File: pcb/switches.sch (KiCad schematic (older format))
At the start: 168 parts

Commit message: correct key sizes
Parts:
- MX_0_1, MX_1_1, MX_2_1, MX_3_1, MX_4_1, MX_5_1, MX_6_1, MX_7_1, MX_8_1, MX_9_1, MX_A_1, MX_B_1, MX_COMMA_1, MX_C_1, MX_DELETE_1, MX_DOT_1, MX_DOWN_1, MX_D_1, MX_END_1, MX_EQUALS_1, MX_ESC_1, MX_E_1, MX_F10_1, MX_F11_1, MX_F12_1, MX_F1_1, MX_F2_1, MX_F3_1, MX_F4_1, MX_F5_1, MX_F6_1, MX_F7_1, MX_F8_1, MX_F9_1, MX_FN_1, MX_F_1, MX_G_1, MX_HOME_1, MX_H_1, MX_I_1, MX_J_1, MX_K_1, MX_LBRAC_1, MX_LEFT_1, MX_L_1, MX_MINUS_1, MX_M_1, MX_N_1, MX_O_1, MX_PAUSE_1, MX_PGDN_1, MX_PGUP_1, MX_PRTSC_1, MX_P_1, MX_QUOTE_1, MX_Q_1, MX_RALT_1, MX_RBRAC_1, MX_RCTRL_1, MX_RIGHT_1, MX_R_1, MX_SEMIC_1, MX_SLASH_1, MX_S_1, MX_TILDE_1, MX_T_1, MX_UP_1, MX_U_1, MX_V_1, MX_W_1, MX_X_1, MX_Y_1, MX_Z_1: footprint (none) -> keys:MX-1U
- MX_BKSPACE_1: footprint (none) -> keys:MX-2U
- MX_BSLSH_1, MX_TAB_1: footprint (none) -> keys:MX-1.5U
- MX_CAPS_1, MX_RSHIFT_1: footprint (none) -> keys:MX-1.75U
- MX_ENTER_1, MX_LSHIFT_1: footprint (none) -> keys:MX-2.25U
- MX_LALT_1, MX_LCTRL_1, MX_OS_1: footprint (none) -> keys:MX-1.25U
- MX_SPACE_1: footprint (none) -> keys:MX-6.25U

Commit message: labels
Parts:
- added R? (x2), R_0_1, R_1_1, R_2_1, R_3_1, R_4_1, R_5_1, R_6_1, R_7_1, R_8_1, R_9_1, R_A_1, R_BKSPACE_1, R_BSLSH_1, R_B_1, R_CAPS_1, R_COMMA_1, R_C_1, R_DELETE_1, R_DOT_1, R_DOWN_1, R_D_1, R_END_1, R_ENTER_1, R_EQUALS_1, R_ESC_1, R_E_1, R_F10_1, R_F11_1, R_F12_1, R_F1_1, R_F2_1, R_F3_1, R_F4_1, R_F5_1, R_F7_1, R_F8_1, R_F9_1, R_FN_1, R_F_1, R_G_1, R_HOME_1, R_H_1, R_I_1, R_J_1, R_K_1, R_LALT_1, R_LBRAC_1, R_LCTRL_1, R_LEFT_1, R_LSHIFT_1, R_L_1, R_MINUS_1, R_M_1, R_N_1, R_OS_1, R_O_1, R_PAUSE_1, R_PGDN_1, R_PGUP_1, R_PRTSC_1, R_P_1, R_QUOTE_1, R_Q_1, R_RALT_1, R_RBRAC_1, R_RCTRL_1, R_RIGHT_1, R_RSHIFT_1, R_R_1, R_SEMIC_1, R_SLASH_1, R_SPACE_1, R_S_1, R_TAB_1, R_TILDE_1, R_T_1, R_UP_1, R_U_1, R_V_1, R_W_1, R_X_1, R_Y_1: R, symbol Device:R
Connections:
- net at MX_ESC_1.3 (LED): now also R_ESC_1.1
- net LEDGND: now reaches MX_ESC_1.4 (LEDGND)
- net LEDGND: now also MX_0_1.4 (LEDGND), MX_1_1.4 (LEDGND), MX_2_1.4 (LEDGND), MX_3_1.4 (LEDGND), MX_4_1.4 (LEDGND), MX_5_1.4 (LEDGND), MX_6_1.4 (LEDGND), MX_7_1.4 (LEDGND), MX_8_1.4 (LEDGND), MX_9_1.4 (LEDGND), MX_A_1.4 (LEDGND), MX_BKSPACE_1.4 (LEDGND), MX_BSLSH_1.4 (LEDGND), MX_B_1.4 (LEDGND), MX_CAPS_1.4 (LEDGND), MX_COMMA_1.4 (LEDGND), MX_C_1.4 (LEDGND), MX_DELETE_1.4 (LEDGND), MX_DOT_1.4 (LEDGND), MX_DOWN_1.4 (LEDGND), MX_D_1.4 (LEDGND), MX_END_1.4 (LEDGND), MX_ENTER_1.4 (LEDGND), MX_EQUALS_1.4 (LEDGND), MX_E_1.4 (LEDGND), MX_F10_1.4 (LEDGND), MX_F11_1.4 (LEDGND), MX_F12_1.4 (LEDGND), MX_F1_1.4 (LEDGND), MX_F2_1.4 (LEDGND), MX_F3_1.4 (LEDGND), MX_F4_1.4 (LEDGND), MX_F5_1.4 (LEDGND), MX_F6_1.4 (LEDGND), MX_F7_1.4 (LEDGND), MX_F8_1.4 (LEDGND), MX_F9_1.4 (LEDGND), MX_FN_1.4 (LEDGND), MX_F_1.4 (LEDGND), MX_G_1.4 (LEDGND), MX_HOME_1.4 (LEDGND), MX_H_1.4 (LEDGND), MX_I_1.4 (LEDGND), MX_J_1.4 (LEDGND), MX_K_1.4 (LEDGND), MX_LALT_1.4 (LEDGND), MX_LBRAC_1.4 (LEDGND), MX_LCTRL_1.4 (LEDGND), MX_LEFT_1.4 (LEDGND), MX_LSHIFT_1.4 (LEDGND), MX_L_1.4 (LEDGND), MX_MINUS_1.4 (LEDGND), MX_M_1.4 (LEDGND), MX_N_1.4 (LEDGND), MX_OS_1.4 (LEDGND), MX_O_1.4 (LEDGND), MX_PAUSE_1.4 (LEDGND), MX_PGDN_1.4 (LEDGND), MX_PGUP_1.4 (LEDGND), MX_PRTSC_1.4 (LEDGND), MX_P_1.4 (LEDGND), MX_QUOTE_1.4 (LEDGND), MX_Q_1.4 (LEDGND), MX_RALT_1.4 (LEDGND), MX_RBRAC_1.4 (LEDGND), MX_RCTRL_1.4 (LEDGND), MX_RIGHT_1.4 (LEDGND), MX_RSHIFT_1.4 (LEDGND), MX_R_1.4 (LEDGND), MX_SEMIC_1.4 (LEDGND), MX_SLASH_1.4 (LEDGND), MX_SPACE_1.4 (LEDGND), MX_S_1.4 (LEDGND), MX_TAB_1.4 (LEDGND), MX_TILDE_1.4 (LEDGND), MX_T_1.4 (LEDGND), MX_UP_1.4 (LEDGND), MX_U_1.4 (LEDGND), MX_V_1.4 (LEDGND), MX_W_1.4 (LEDGND), MX_X_1.4 (LEDGND), MX_Y_1.4 (LEDGND), MX_Z_1.4 (LEDGND)
- net at MX_F1_1.3 (LED): now also R_F1_1.1
- net at MX_F2_1.3 (LED): now also R_F2_1.1
- net at MX_F3_1.3 (LED): now also R_F3_1.1
- net at MX_F4_1.3 (LED): now also R_F4_1.1
- net at MX_F5_1.3 (LED): now also R_F5_1.1
- net at MX_F6_1.3 (LED): now also R?.1
- net at MX_F7_1.3 (LED): now also R_F7_1.1
- net at MX_F8_1.3 (LED): now also R_F8_1.1
- net at MX_F9_1.3 (LED): now also R_F9_1.1
- net at MX_F10_1.3 (LED): now also R_F10_1.1
- net at MX_F11_1.3 (LED): now also R_F11_1.1
- net at MX_F12_1.3 (LED): now also R_F12_1.1
- net at MX_PRTSC_1.3 (LED): now also R_PRTSC_1.1
- net at MX_PAUSE_1.3 (LED): now also R_PAUSE_1.1
- net at MX_DELETE_1.3 (LED): now also R_DELETE_1.1
- net at MX_TILDE_1.3 (LED): now also R_TILDE_1.1
- net at MX_1_1.3 (LED): now also R_1_1.1
- net at MX_2_1.3 (LED): now also R_2_1.1
- net at MX_3_1.3 (LED): now also R_3_1.1
- net at MX_4_1.3 (LED): now also R_4_1.1
- net at MX_5_1.3 (LED): now also R_5_1.1
- net at MX_6_1.3 (LED): now also R_6_1.1
- net at MX_7_1.3 (LED): now also R_7_1.1
- net at MX_8_1.3 (LED): now also R_8_1.1
- net at MX_9_1.3 (LED): now also R_9_1.1
- net at MX_0_1.3 (LED): now also R_0_1.1
- net at MX_MINUS_1.3 (LED): now also R_MINUS_1.1
- net at MX_EQUALS_1.3 (LED): now also R_EQUALS_1.1
- net at MX_BKSPACE_1.3 (LED): now also R_BKSPACE_1.1
- net at MX_HOME_1.3 (LED): now also R_HOME_1.1
- net at MX_TAB_1.3 (LED): now also R_TAB_1.1
- net at MX_Q_1.3 (LED): now also R_Q_1.1
- net at MX_W_1.3 (LED): now also R_W_1.1
- net at MX_E_1.3 (LED): now also R_E_1.1
- net at MX_R_1.3 (LED): now also R_R_1.1
- net at MX_T_1.3 (LED): now also R_T_1.1
- net at MX_Y_1.3 (LED): now also R_Y_1.1
- net at MX_U_1.3 (LED): now also R_U_1.1
- net at MX_I_1.3 (LED): now also R_I_1.1
- net at MX_O_1.3 (LED): now also R_O_1.1
- net at MX_P_1.3 (LED): now also R_P_1.1
- net at MX_LBRAC_1.3 (LED): now also R_LBRAC_1.1
- net at MX_RBRAC_1.3 (LED): now also R_RBRAC_1.1
- net at MX_BSLSH_1.3 (LED): now also R_BSLSH_1.1
- net at MX_PGUP_1.3 (LED): now also R_PGUP_1.1
- net at MX_CAPS_1.3 (LED): now also R_CAPS_1.1
- net at MX_A_1.3 (LED): now also R_A_1.1
- net at MX_S_1.3 (LED): now also R_S_1.1
- net at MX_D_1.3 (LED): now also R_D_1.1
- net at MX_F_1.3 (LED): now also R_F_1.1
- net at MX_G_1.3 (LED): now also R_G_1.1
- net at MX_H_1.3 (LED): now also R_H_1.1
- net at MX_J_1.3 (LED): now also R_J_1.1
- net at MX_K_1.3 (LED): now also R_K_1.1
- net at MX_L_1.3 (LED): now also R_L_1.1
- net at MX_SEMIC_1.3 (LED): now also R_SEMIC_1.1
- net at MX_QUOTE_1.3 (LED): now also R_QUOTE_1.1
- net at MX_ENTER_1.3 (LED): now also R_ENTER_1.1
- net at MX_PGDN_1.3 (LED): now also R_PGDN_1.1
- net at MX_LSHIFT_1.3 (LED): now also R_LSHIFT_1.1
- net at MX_Z_1.3 (LED): now also R?.1
- net at MX_X_1.3 (LED): now also R_X_1.1
- net at MX_C_1.3 (LED): now also R_C_1.1
- net at MX_V_1.3 (LED): now also R_V_1.1
- net at MX_B_1.3 (LED): now also R_B_1.1
- net at MX_N_1.3 (LED): now also R_N_1.1
- net at MX_M_1.3 (LED): now also R_M_1.1
- net at MX_COMMA_1.3 (LED): now also R_COMMA_1.1
- net at MX_DOT_1.3 (LED): now also R_DOT_1.1
- net at MX_SLASH_1.3 (LED): now also R_SLASH_1.1
- net at MX_RSHIFT_1.3 (LED): now also R_RSHIFT_1.1
- net at MX_UP_1.3 (LED): now also R_UP_1.1
- net at MX_END_1.3 (LED): now also R_END_1.1
- net at MX_LCTRL_1.3 (LED): now also R_LCTRL_1.1
- net at MX_OS_1.3 (LED): now also R_OS_1.1
- net at MX_LALT_1.3 (LED): now also R_LALT_1.1
- net at MX_SPACE_1.3 (LED): now also R_SPACE_1.1
- net at MX_RALT_1.3 (LED): now also R_RALT_1.1
- net at MX_FN_1.3 (LED): now also R_FN_1.1
- net at MX_RCTRL_1.3 (LED): now also R_RCTRL_1.1
- net at MX_LEFT_1.3 (LED): now also R_LEFT_1.1
- net at MX_DOWN_1.3 (LED): now also R_DOWN_1.1
- net at MX_RIGHT_1.3 (LED): now also R_RIGHT_1.1
- new net 5V: R?.2, R?.2, R_0_1.2, R_1_1.2, R_2_1.2, R_3_1.2, R_4_1.2, R_5_1.2, R_6_1.2, R_7_1.2, R_8_1.2, R_9_1.2, R_A_1.2, R_BKSPACE_1.2, R_BSLSH_1.2, R_B_1.2, R_CAPS_1.2, R_COMMA_1.2, R_C_1.2, R_DELETE_1.2, R_DOT_1.2, R_DOWN_1.2, R_D_1.2, R_END_1.2, R_ENTER_1.2, R_EQUALS_1.2, R_ESC_1.2, R_E_1.2, R_F10_1.2, R_F11_1.2, R_F12_1.2, R_F1_1.2, R_F2_1.2, R_F3_1.2, R_F4_1.2, R_F5_1.2, R_F7_1.2, R_F8_1.2, R_F9_1.2, R_FN_1.2, R_F_1.2, R_G_1.2, R_HOME_1.2, R_H_1.2, R_I_1.2, R_J_1.2, R_K_1.2, R_LALT_1.2, R_LBRAC_1.2, R_LCTRL_1.2, R_LEFT_1.2, R_LSHIFT_1.2, R_L_1.2, R_MINUS_1.2, R_M_1.2, R_N_1.2, R_OS_1.2, R_O_1.2, R_PAUSE_1.2, R_PGDN_1.2, R_PGUP_1.2, R_PRTSC_1.2, R_P_1.2, R_QUOTE_1.2, R_Q_1.2, R_RALT_1.2, R_RBRAC_1.2, R_RCTRL_1.2, R_RIGHT_1.2, R_RSHIFT_1.2, R_R_1.2, R_SEMIC_1.2, R_SLASH_1.2, R_SPACE_1.2, R_S_1.2, R_TAB_1.2, R_TILDE_1.2, R_T_1.2, R_UP_1.2, R_U_1.2, R_V_1.2, R_W_1.2, R_X_1.2, R_Y_1.2

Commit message: led resistor values
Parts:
- R? (x2), R_0_1, R_1_1, R_2_1, R_3_1, R_4_1, R_5_1, R_6_1, R_7_1, R_8_1, R_9_1, R_A_1, R_BKSPACE_1, R_BSLSH_1, R_B_1, R_CAPS_1, R_COMMA_1, R_C_1, R_DELETE_1, R_DOT_1, R_DOWN_1, R_D_1, R_END_1, R_ENTER_1, R_EQUALS_1, R_ESC_1, R_E_1, R_F10_1, R_F11_1, R_F12_1, R_F1_1, R_F2_1, R_F3_1, R_F4_1, R_F5_1, R_F7_1, R_F8_1, R_F9_1, R_FN_1, R_F_1, R_G_1, R_HOME_1, R_H_1, R_I_1, R_J_1, R_K_1, R_LALT_1, R_LBRAC_1, R_LCTRL_1, R_LEFT_1, R_LSHIFT_1, R_L_1, R_MINUS_1, R_M_1, R_N_1, R_OS_1, R_O_1, R_PAUSE_1, R_PGDN_1, R_PGUP_1, R_PRTSC_1, R_P_1, R_QUOTE_1, R_Q_1, R_RALT_1, R_RBRAC_1, R_RCTRL_1, R_RIGHT_1, R_RSHIFT_1, R_R_1, R_SEMIC_1, R_SLASH_1, R_SPACE_1, R_S_1, R_TAB_1, R_TILDE_1, R_T_1, R_UP_1, R_U_1, R_V_1, R_W_1, R_X_1, R_Y_1: value R -> 470

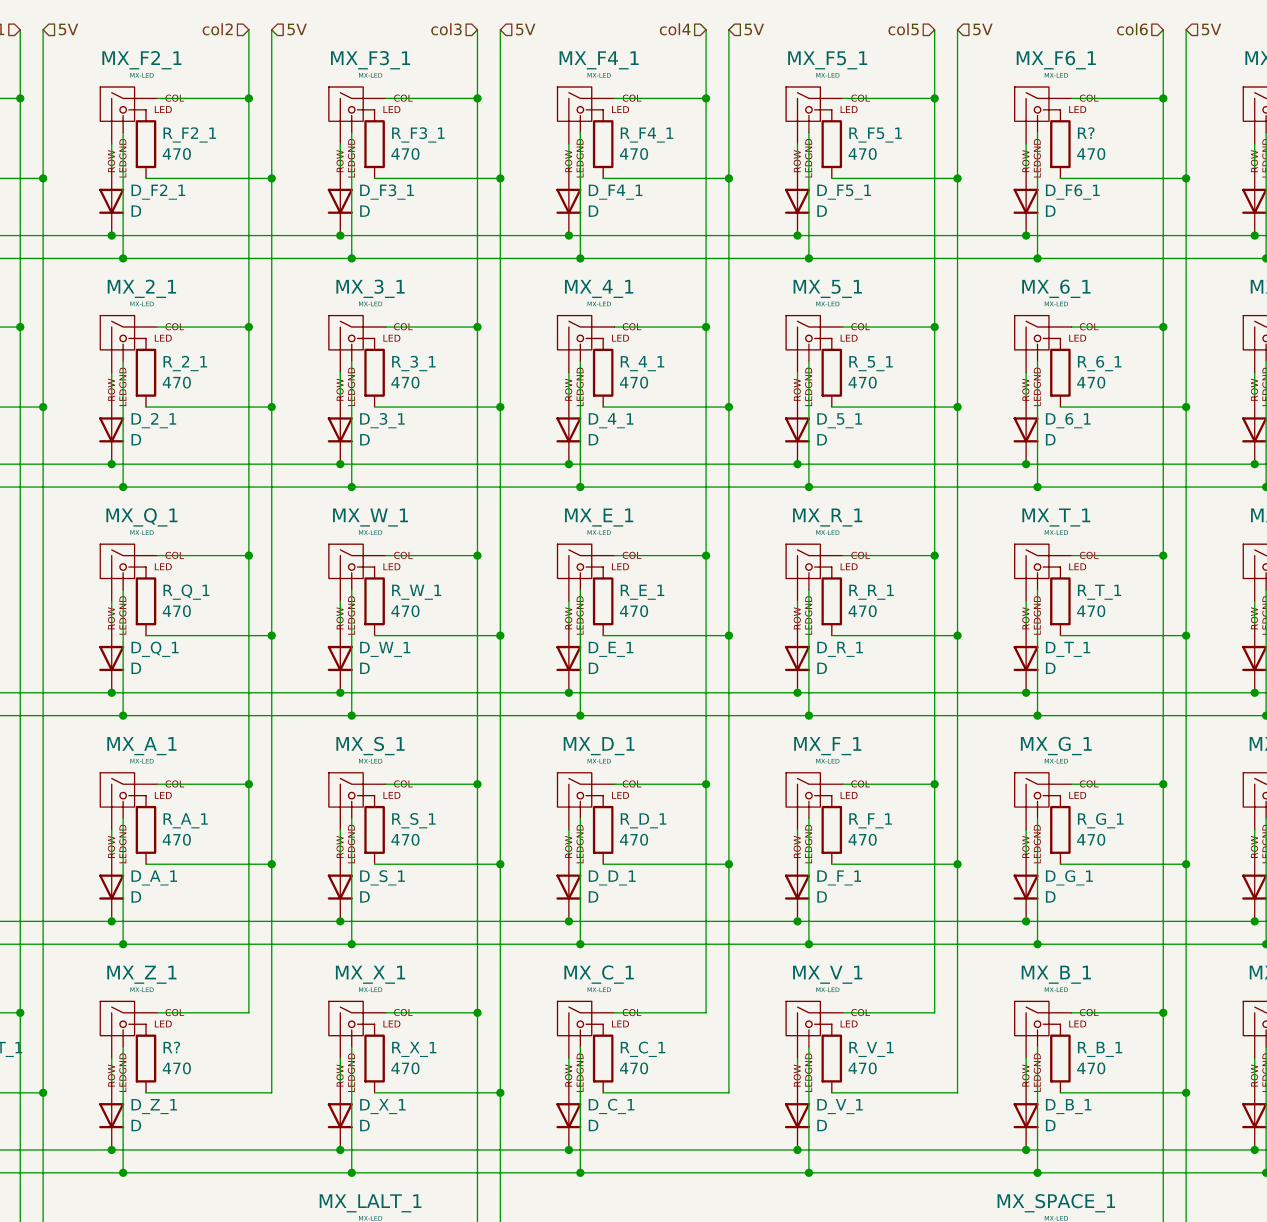
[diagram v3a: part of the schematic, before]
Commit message: Resistor footprints
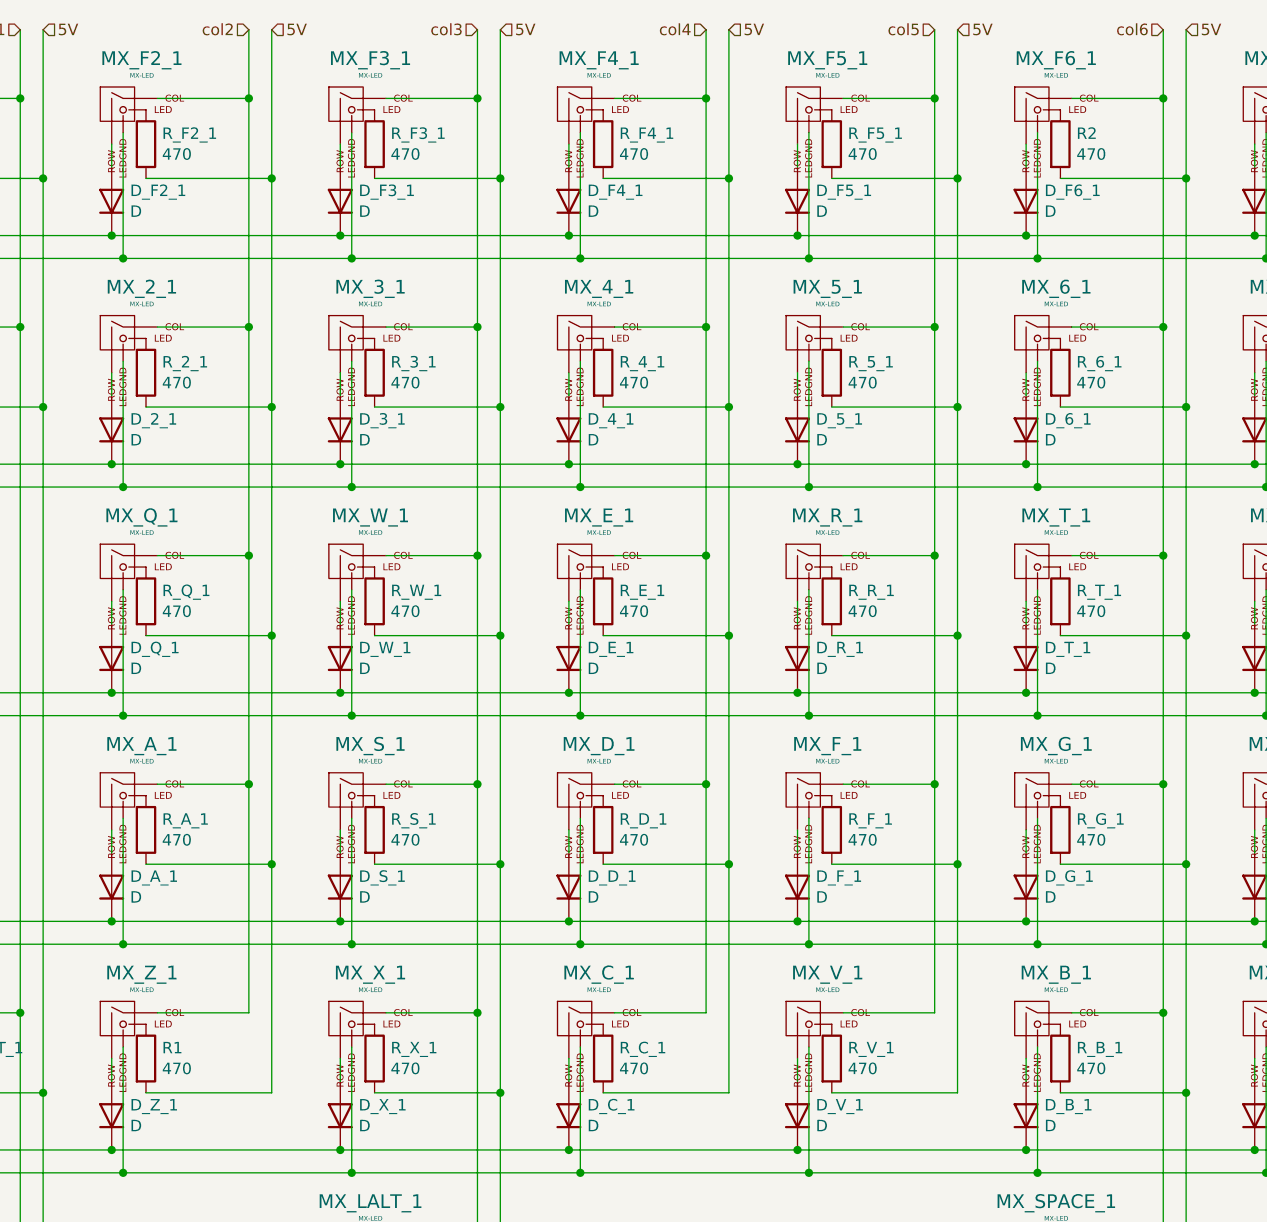
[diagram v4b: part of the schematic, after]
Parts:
- R1, R2: renamed from R?; footprint (none) -> Resistor_THT:R_Axial_DIN0207_L6.3mm_D2.5mm_P7.62mm_Horizontal
- R_0_1, R_1_1, R_2_1, R_3_1, R_4_1, R_5_1, R_6_1, R_7_1, R_8_1, R_9_1, R_A_1, R_BKSPACE_1, R_BSLSH_1, R_B_1, R_CAPS_1, R_COMMA_1, R_C_1, R_DELETE_1, R_DOT_1, R_DOWN_1, R_D_1, R_END_1, R_ENTER_1, R_EQUALS_1, R_ESC_1, R_E_1, R_F10_1, R_F11_1, R_F12_1, R_F1_1, R_F2_1, R_F3_1, R_F4_1, R_F5_1, R_F7_1, R_F8_1, R_F9_1, R_FN_1, R_F_1, R_G_1, R_HOME_1, R_H_1, R_I_1, R_J_1, R_K_1, R_LALT_1, R_LBRAC_1, R_LCTRL_1, R_LEFT_1, R_LSHIFT_1, R_L_1, R_MINUS_1, R_M_1, R_N_1, R_OS_1, R_O_1, R_PAUSE_1, R_PGDN_1, R_PGUP_1, R_PRTSC_1, R_P_1, R_QUOTE_1, R_Q_1, R_RALT_1, R_RBRAC_1, R_RCTRL_1, R_RIGHT_1, R_RSHIFT_1, R_R_1, R_SEMIC_1, R_SLASH_1, R_SPACE_1, R_S_1, R_TAB_1, R_TILDE_1, R_T_1, R_UP_1, R_U_1, R_V_1, R_W_1, R_X_1, R_Y_1: footprint (none) -> Resistor_THT:R_Axial_DIN0207_L6.3mm_D2.5mm_P7.62mm_Horizontal

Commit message: missing connection
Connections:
- net col7: now also MX_F7_1.1 (COL)
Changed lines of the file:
@@
 	9600 5150 9600 6150
 Wire Wire Line
-	11600 4850 11600 6150
+	11600 4850 11600 5150
 Wire Wire Line
 	10200 5150 10600 5150
@@
 	1    0    0    -1
 $EndComp
+Wire Wire Line
+	11200 5150 11600 5150
+Connection ~ 11600 5150
+Wire Wire Line
+	11600 5150 11600 6150
 $EndSCHEMATC

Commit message: first layout
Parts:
- renumbered R2 to R_F6_1, R1 to R_Z_1
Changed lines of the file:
@@
 $EndComp
 $Comp
-L Device:R R2
+L Device:R R_F6_1
 U 1 1 611BC026
 P 10150 5350
-F 0 "R2" H 10220 5396 50  0000 L CNN
+F 0 "R_F6_1" H 10220 5396 50  0000 L CNN
 F 1 "470" H 10220 5305 50  0000 L CNN
 F 2 "Resistor_THT:R_Axial_DIN0207_L6.3mm_D2.5mm_P7.62mm_Horizontal" V 10080 5350 50  0001 C CNN
@@
 $EndComp
 $Comp
-L Device:R R1
+L Device:R R_Z_1
 U 1 1 611CF8B4
 P 6150 9350
-F 0 "R1" H 6220 9396 50  0000 L CNN
+F 0 "R_Z_1" H 6220 9396 50  0000 L CNN
 F 1 "470" H 6220 9305 50  0000 L CNN
 F 2 "Resistor_THT:R_Axial_DIN0207_L6.3mm_D2.5mm_P7.62mm_Horizontal" V 6080 9350 50  0001 C CNN

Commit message: reversed stabs
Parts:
- MX_BKSPACE_1: footprint keys:MX-2U -> keys:MX-2U-ReversedStabilizers
- MX_ENTER_1, MX_LSHIFT_1: footprint keys:MX-2.25U -> keys:MX-2.25U-ReversedStabilizers
- MX_SPACE_1: footprint keys:MX-6.25U -> keys:MX-6.25U-ReversedStabilizers
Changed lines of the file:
@@
 F 0 "MX_BKSPACE_1" H 18132 6424 60  0000 C CNN
 F 1 "MX-LED" H 18132 6350 20  0000 C CNN
-F 2 "keys:MX-2U" H 17425 6175 60  0001 C CNN
+F 2 "keys:MX-2U-ReversedStabilizers" H 17425 6175 60  0001 C CNN
 F 3 "" H 17425 6175 60  0001 C CNN
 	1    18050 6200
@@
 F 0 "MX_ENTER_1" H 17132 8424 60  0000 C CNN
 F 1 "MX-LED" H 17132 8350 20  0000 C CNN
-F 2 "keys:MX-2.25U" H 16425 8175 60  0001 C CNN
+F 2 "keys:MX-2.25U-ReversedStabilizers" H 16425 8175 60  0001 C CNN
 F 3 "" H 16425 8175 60  0001 C CNN
 	1    17050 8200
@@
 F 0 "MX_LSHIFT_1" H 5132 9424 60  0000 C CNN
 F 1 "MX-LED" H 5132 9350 20  0000 C CNN
-F 2 "keys:MX-2.25U" H 4425 9175 60  0001 C CNN
+F 2 "keys:MX-2.25U-ReversedStabilizers" H 4425 9175 60  0001 C CNN
 F 3 "" H 4425 9175 60  0001 C CNN
 	1    5050 9200
@@
 F 0 "MX_SPACE_1" H 10132 10424 60  0000 C CNN
 F 1 "MX-LED" H 10132 10350 20  0000 C CNN
-F 2 "keys:MX-6.25U" H 9425 10175 60  0001 C CNN
+F 2 "keys:MX-6.25U-ReversedStabilizers" H 9425 10175 60  0001 C CNN
 F 3 "" H 9425 10175 60  0001 C CNN
 	1    10050 10200

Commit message: reversed space stab
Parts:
- MX_SPACE_1: footprint keys:MX-6.25U-ReversedStabilizers -> keys:MX-6.25U
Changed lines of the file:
@@
 F 0 "MX_SPACE_1" H 10132 10424 60  0000 C CNN
 F 1 "MX-LED" H 10132 10350 20  0000 C CNN
-F 2 "keys:MX-6.25U-ReversedStabilizers" H 9425 10175 60  0001 C CNN
+F 2 "keys:MX-6.25U" H 9425 10175 60  0001 C CNN
 F 3 "" H 9425 10175 60  0001 C CNN
 	1    10050 10200
